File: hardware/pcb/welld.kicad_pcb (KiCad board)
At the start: 2 copper layers, 80 x 55 mm, 126 parts, among them J1 LiPo, J10 PROG, J12 Solar, J2 USB-C, J3 U.FL, J4 4-20mA_1, J5 4-20mA_2, J6 DS18B20, J7 Spare, J8 I2C, J9 GPIO, Q1 BSS123, Q2 BSS123, Q3 BSS84, SW1 RESET, SW2 BOOT, U1 TPS7A0533, U10 MAX17048, U2 TP4056, U3 S-8261A, U4 FS8205A, U5 USBLC6, U6 ESP32-C6, U7 CN3791, U8 TPS61023, U9 ADS1115

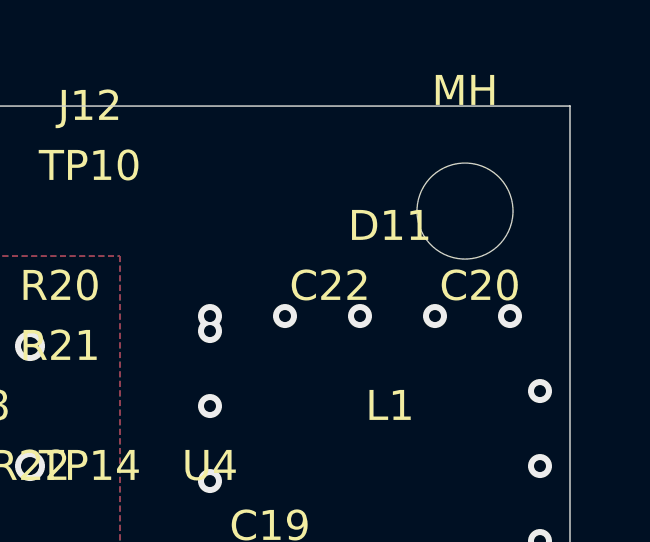
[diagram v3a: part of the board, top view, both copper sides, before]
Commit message: feat(pcb): generate KiCad 10-compatible schematic with working GUI symbol rendering
Rewrote generate_kicad.py to produce lib_symbols entries with the full
"Library:Name" prefix required by KiCad 10's GUI (e.g. "Device:R",
"welld:AP63205WU", "power:VBAT"). kicad-cli tolerates bare names but
the GUI showed "??" for every symbol without the prefix.

Also adds: stdlib symbol embedding (_extract_sym + _STDLIB_NEEDED),
custom VBAT power symbol, welld.kicad_sym library file, project-level
sym-lib-table with absolute paths, and kicad-cli post-upgrade step.

Removes stale jlcpcb_bom.csv / jlcpcb_cpl.csv (superseded by welld_bom.csv).

Co-Authored-By: Claude Sonnet 4.6 <noreply@anthropic.com>
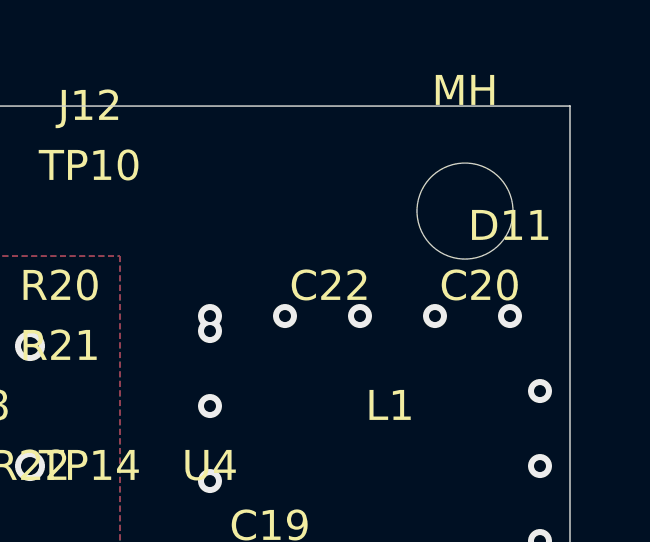
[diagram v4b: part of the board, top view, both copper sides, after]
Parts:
- moved D11 4.00 mm to (78.0, 6.00)
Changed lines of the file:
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@@
-(kicad_pcb (version 20221018) (generator "welld_generate_kicad")
+(kicad_pcb (version 20260206) (generator "pcbnew") (generator_version "10.0")
   (general
     (thickness 1.6)
@@
   (paper "A3")
   (title_block
-    (title "WellD Well-Level Monitor PCB — 2S 18650 LiPo")
+    (title "WellD Well-Level Monitor PCB")
     (date "2026-05-18")
     (company "WellD Project")
@@
   (net 2 "+3V3")
   (net 3 "VBAT")
+  (net 4 "VUSB")
+  (net 5 "VUSB_IN")
   (net 6 "VSOLAR")
   (net 7 "VSOLAR_IN")
@@
   (net 18 "BOOT")
   (net 19 "MPPT_REF")
+  (net 20 "/CHRG_USB")
+  (net 21 "/DONE_USB")
   (net 22 "/CHRG_SOLAR")
+  (net 23 "/DONE_SOLAR")
   (net 24 "VLOOP")
   (net 25 "VBOOST_EN")
+  (net 26 "CHRG_USB_DIS")
   (net 27 "SOLAR_DET")
   (net 28 "BATT_DIV_EN")
   (net 29 "ADS_DRDY")
+  (net 30 "MAX_ALRT")
   (net 31 "LOOP_TERM_CH1")
   (net 32 "LOOP_TERM_CH2")
@@
     )
   )
-  (footprint "Diode_SMD:D_SMA" (layer "F.Cu") (at 74.000 6.000 0.0)
+  (footprint "Diode_SMD:D_SMA" (layer "F.Cu") (at 78.000 6.000 0.0)
     (property "Reference" "D11" (at 0 -2 0) (layer "F.SilkS")
       (effects (font (size 1 1) (thickness 0.15)))
@@
     (connect_pads thru_hole_only (clearance 0.2))
     (min_thickness 0.25)
-    (keepout_settings (no_tracks no) (no_vias no) (no_pads no) (no_copperpour no) (no_footprints no))
     (fill yes (thermal_gap 0.3) (thermal_bridge_width 0.3))
     (polygon
@@
     (connect_pads thru_hole_only (clearance 0.2))
     (min_thickness 0.25)
-    (keepout_settings (no_tracks no) (no_vias no) (no_pads no) (no_copperpour no) (no_footprints no))
     (fill yes (thermal_gap 0.3) (thermal_bridge_width 0.3))
     (polygon

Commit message: hw(pcb): full placement pass, XT30 connector, SMA antenna, BOM cleanup
Component placement:
- All 116 components placed inside 80×55 mm board outline
- pcbway_cpl.csv fully rewritten with correct board-relative coordinates

Battery connector (J1):
- Changed from JST PH 2.0mm to AMASS XT30PW-F right-angle THT (LCSC C601498)
- Pad drill corrected 1.5 mm → 1.8 mm for IPC-2221 wave-solder clearance

Antenna (J3 + W1):
- J3: Amphenol 132289 SMD edge-launch SMA on bottom board edge
- W1: Taoglas CAB.100.07.0050B ~50 mm U.FL-to-SMA pigtail (hand-attached post-reflow)
- RF_ANT net assigned to J3 signal pad

Inductor L2:
- Footprint corrected from L_2512_6332Metric to L_Vishay_IFSC-1515AH_4x4x1.8mm
- Now matches MPN CDRH4D22NP-4R7NC body; shares footprint, reel, and LCSC C376098 with L1

VLOOP output caps (C20, C22):
- Voltage rating upgraded 16 V → 25 V (2.1× margin on 12 V rail; proper DC-bias headroom)
- Footprints unchanged (1206 / 0805)

BOM cleanup:
- J8, J9: marked DNF (expansion headers not populated in production)
- J4–J7, J12, J10: Package updated to THT; PCBWay wave-solders

Case:
- XT30PW-F left-wall cutout added: 14×12 mm slot at Y=17–31 mm, Z=19.3–31.3 mm
- SMA bottom-wall cutout (10.5 mm ⌀ at X=42.5 mm) confirmed present

Co-Authored-By: Claude Sonnet 4.6 <noreply@anthropic.com>
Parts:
- removed C1, C2: 10uF, Capacitor_SMD:C_0805_2012Metric
- removed C16: 4.7uF, Capacitor_SMD:C_0805_2012Metric
- removed C25, C26: 100nF, Capacitor_SMD:C_0402_1005Metric
- removed D2: LED_CHRG, LED_SMD:LED_0603_1608Metric
- removed D3: LED_STBY, LED_SMD:LED_0603_1608Metric
- removed F1: PTC_1A, Fuse:Fuse_1206_3216Metric
- removed J2: USB-C, welld:USB_C_9x3.2mm
- removed the MH at (3.50, 3.50)
- removed the MH at (76.5, 3.50)
- removed the MH at (3.50, 51.5)
- removed the MH at (76.5, 51.5)
- removed Q1: BSS123, Package_TO_SOT_SMD:SOT-23
- removed Q3: BSS84, Package_TO_SOT_SMD:SOT-23
- removed R1: 2k0, Resistor_SMD:R_0402_1005Metric
- removed R15, R16: 5k1, Resistor_SMD:R_0402_1005Metric
- removed R17, R18: 1k_DNF, Resistor_SMD:R_0402_1005Metric
- removed R25, R27, R29: 4k7, Resistor_SMD:R_0402_1005Metric
- removed R30: 10k, Resistor_SMD:R_0402_1005Metric
- removed TP13: MAX_ALRT, TestPoint:TestPoint_Pad_1.0x1.0mm
- removed U10: MAX17048, Package_TO_SOT_SMD:SOT-23-6
- removed U2: TP4056, Package_SO:SOIC-8_3.9x4.9mm_P1.27mm
- removed U3: S-8261A, Package_TO_SOT_SMD:SOT-23-6
- removed U4: FS8205A, Package_TO_SOT_SMD:SOT-23-6
- removed U5: USBLC6, Package_TO_SOT_SMD:SOT-23-6
- added C27: 4.7uF, Capacitor_SMD:C_0805_2012Metric, F.Cu at (90.0, 74.5)
- added C28: 10uF, Capacitor_SMD:C_0805_2012Metric, F.Cu at (93.0, 86.5)
- added C29: 10uF, Capacitor_SMD:C_0805_2012Metric, F.Cu at (93.0, 90.5)
- added C_BST: 100nF, Capacitor_SMD:C_0402_1005Metric, F.Cu at (101.0, 85.5)
- added C_BUCK: 10uF, Capacitor_SMD:C_0805_2012Metric, F.Cu at (90.0, 81.5)
- added D12: PRTR5V, Package_TO_SOT_SMD:SOT-363_SC-70-6, F.Cu at (122.0, 82.5)
- added D13: SMAJ10CA, Diode_SMD:D_SMA, F.Cu at (71.0, 86.5)
- added D14: SMAJ28CA, Diode_SMD:D_SMA, F.Cu at (130.0, 52.5)
- added F2: Polyfuse, Fuse:Fuse_1206_3216Metric, F.Cu at (90.0, 70.5)
- added J13: USB-C, Connector_USB:USB_C_Receptacle_GCT_USB4135-GF-A_6P_TopMnt_Horizontal, F.Cu at (70.0, 71.5)
- added L2: 4.7uH, Inductor_SMD:L_Vishay_IFSC-1515AH_4x4x1.8mm, F.Cu at (82.0, 80.5)
- added MH: MountingHole_3.2mm_M3, MountingHole:MountingHole_3.2mm_M3, F.Cu at (68.5, 50.0)
- added MH: MountingHole_3.2mm_M3, MountingHole:MountingHole_3.2mm_M3, F.Cu at (141.5, 50.0)
- added MH: MountingHole_3.2mm_M3, MountingHole:MountingHole_3.2mm_M3, F.Cu at (68.5, 98.0)
- added MH: MountingHole_3.2mm_M3, MountingHole:MountingHole_3.2mm_M3, F.Cu at (141.5, 98.0)
- added R33: 604k, Resistor_SMD:R_0402_1005Metric, F.Cu at (92.0, 60.5)
- added R34: 100k, Resistor_SMD:R_0402_1005Metric, F.Cu at (92.0, 64.5)
- added R35: 1k2, Resistor_SMD:R_0402_1005Metric, F.Cu at (81.0, 86.5)
- added R36: 100k, Resistor_SMD:R_0402_1005Metric, F.Cu at (81.0, 90.5)
- added R37: 4k7, Resistor_SMD:R_0402_1005Metric, F.Cu at (81.0, 94.5)
- added R38: 4k7, Resistor_SMD:R_0402_1005Metric, F.Cu at (86.0, 94.5)
- added R_CC1: 5k1, Resistor_SMD:R_0402_1005Metric, F.Cu at (78.0, 69.5)
- added R_CC2: 5k1, Resistor_SMD:R_0402_1005Metric, F.Cu at (78.0, 72.5)
- added TP15: CHRG_USB, TestPoint:TestPoint_Pad_1.0x1.0mm, F.Cu at (132.0, 98.5)
- added U11: USBLC6, Package_TO_SOT_SMD:SOT-23-6, F.Cu at (84.0, 70.5)
- added U12: TP5100, Package_SO:SOIC-8_3.9x4.9mm_P1.27mm, F.Cu at (86.0, 89.5)
- C20: value 22uF -> 22uF 25V
- C22: value 10uF -> 10uF 25V
- D1: value PRTR5V0U2X -> PRTR5V
- D10, D9: value SMAJ3.3CA -> SMAJ3.3
- D11: value SMAJ13A -> SMAJ13
- D4: value LED_STATUS -> Status
- D7: value LED_SOLAR -> LED
- D8: value SMAJ7.0A -> SMAJ28CA
- FB1: value 600R@100MHz -> Ferrite; footprint Ferrite_Bead_SMD:L_0402_1005Metric -> Inductor_SMD:L_0402_1005Metric
- J1: value LiPo -> XT30PW-F; footprint Connector_JST:JST_XH_B2B-XH-AM_1x02_P2.50mm_Horizontal -> WellD:XT30PW-F_RightAngle
- J12: footprint Connector_Phoenix_MC:PhoenixContact_MC_1,5_2-G-3,5_1x02_P3.50mm_Horizontal -> TerminalBlock_Phoenix:TerminalBlock_Phoenix_PT-1,5-2-3.5-H_1x02_P3.50mm_Horizontal
- J3: value U.FL -> 132289; footprint Connector_Coaxial:U.FL_Hirose_U.FL-R-SMT-1_Vertical -> Connector_Coaxial:SMA_Amphenol_132289_EdgeMount
- J4, J5, J6, J7: footprint Connector_Phoenix_MC:PhoenixContact_MC_1,5_3-G-3,5_1x03_P3.50mm_Horizontal -> TerminalBlock_Phoenix:TerminalBlock_Phoenix_PT-1,5-3-3.5-H_1x03_P3.50mm_Horizontal
- L1: footprint Inductor_SMD:L_1812_4532Metric -> Inductor_SMD:L_Vishay_IFSC-1515AH_4x4x1.8mm
- R2, R4: value 100R_0.1% -> 100R
- R22: value 1k_DNF -> 1k DNF
- R23: value 1.1M -> 1.91M
- R24: value 47k -> 100k
- R32: value 33R_DNF -> 33R
- R7: value 100k -> 330k
- SJ1: value VBOOST_EN -> VBOOST; footprint Jumper:SolderJumper-2_P1.3mm_Open_RoundedPad1.0x1.5mm -> Jumper:SolderJumper-2_P1.3mm_Open_Pad1.0x1.5mm
- SJ2: value VLOOP_BUS -> VLOOP; footprint Jumper:SolderJumper-2_P1.3mm_Open_RoundedPad1.0x1.5mm -> Jumper:SolderJumper-2_P1.3mm_Open_Pad1.0x1.5mm
- SJ3, SJ4, SJ5: footprint Jumper:SolderJumper-2_P1.3mm_Open_RoundedPad1.0x1.5mm -> Jumper:SolderJumper-2_P1.3mm_Open_Pad1.0x1.5mm
- SW1, SW2: footprint Button_Switch_SMD:SW_SPST_TL3305AF160QG -> Button_Switch_SMD:SW_Push_1P1T_NO_CK_KSC6xxG
- TP10: value VSOLAR_IN -> VSOLAR
- TP14: value /CHRG_SOLAR -> CHRG_SOL
- TP5: value LOOP_TERM_CH1 -> LOOP1
- TP6: value LOOP_TERM_CH2 -> LOOP2
- TP8: value I2C_SDA -> SDA
- TP9: value I2C_SCL -> SCL
- U1: value TPS7A0533 -> AP63205; footprint Package_TO_SOT_SMD:SC-70-5 -> Package_TO_SOT_SMD:SOT-23-6
- U6: footprint welld:ESP32_C6_MINI_1U -> PCM_Espressif:ESP32-C6-MINI-1U
- U7: value CN3791 -> CN3722
- U8: value TPS61023 -> MT3608; footprint Package_TO_SOT_SMD:SOT-23-5 -> Package_TO_SOT_SMD:SOT-23-6
- moved J9 297.4 mm to (265.0, 256.5)
- moved J8 279.7 mm to (265.0, 246.5)
- moved J4 140.6 mm to (138.0, 64.5), turned to 180 degrees
- moved J5 137.0 mm to (138.0, 76.5), turned to 180 degrees
- moved J6 135.3 mm to (138.0, 88.5), turned to 180 degrees
- moved SJ4 132.9 mm to (118.0, 90.5)
- moved J7 132.6 mm to (138.0, 96.5), turned to 180 degrees
- moved R2 131.8 mm to (129.0, 79.5)
- moved D9 131.5 mm to (123.0, 76.5)
- moved SJ5 130.7 mm to (118.0, 94.5)
- moved SJ2 129.8 mm to (113.0, 94.5)
- moved C_SH1 129.2 mm to (129.0, 76.5)
- moved R4 128.9 mm to (129.0, 87.5)
- moved D10 127.1 mm to (123.0, 84.5)
- moved C4 127.0 mm to (129.0, 82.5)
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
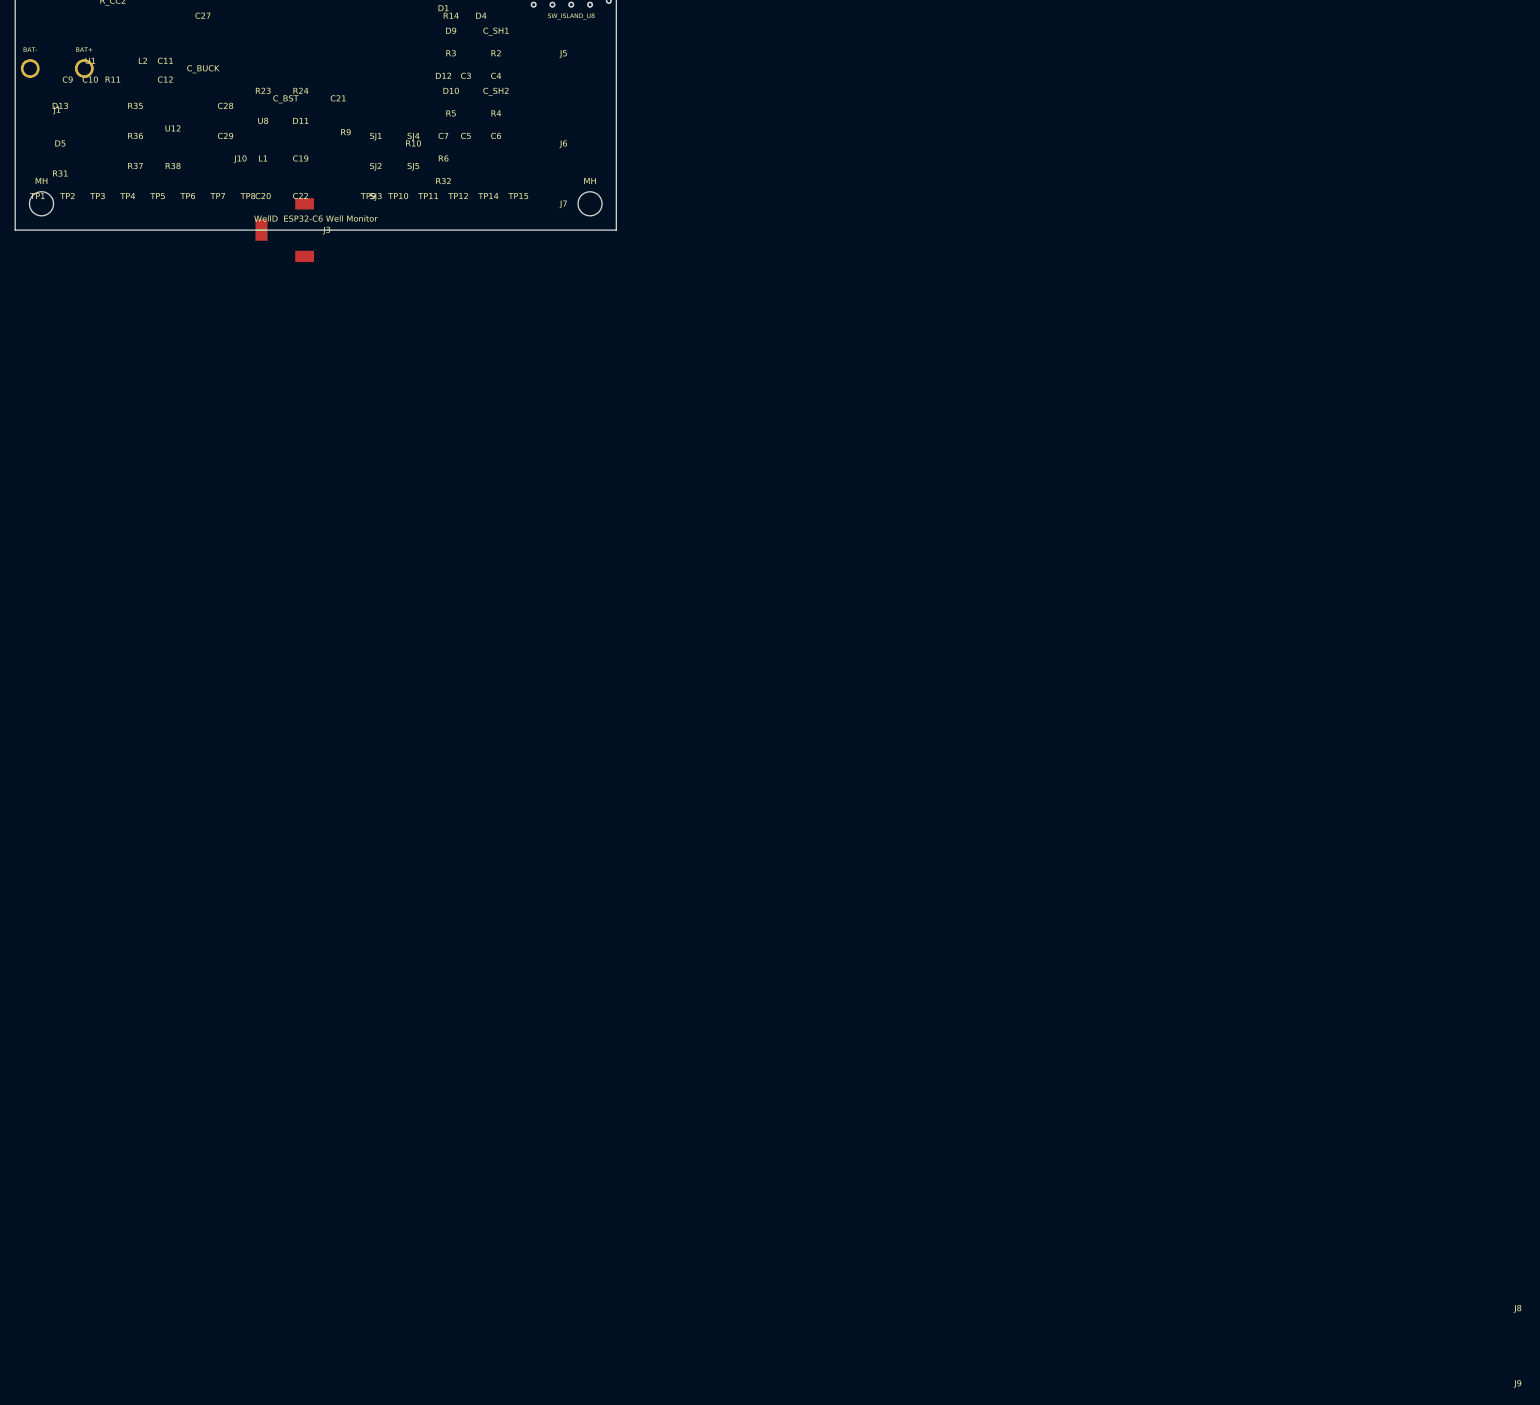
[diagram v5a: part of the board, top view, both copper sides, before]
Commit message: hw(pcb): fix J1 XT30 placement — rotation 270°, correct pad names/drill
The community AMASS_XT30PW-M footprint has pads at y=10mm (10mm from
the connector face) and 5mm pin pitch. To mount at the left wall with
the mating face pointing outward, J1 needs rotation 270°, not 180°.

- Footprint: rename pads P→1, N→2 to match schematic pin numbers;
  drill 1.7→1.8mm (our IPC-2221 spec)
- generate_kicad.py: J1 board pos (5.6,33.5)→(2.0,33.5), rot 180→270;
  update courtyard keepout comment
- Regenerate welld.kicad_pcb: J1 now at PCB (67,80) @270°

At 270° from board (2,33.5): mating face at board x≈-1mm (accessible
through left-wall case cutout), power pins at board (12,31)+(12,36),
courtyard X -1.2..13.5, Y 26.6..40.4. Case cutout Y unchanged.

Co-Authored-By: Claude Sonnet 4.6 <noreply@anthropic.com>
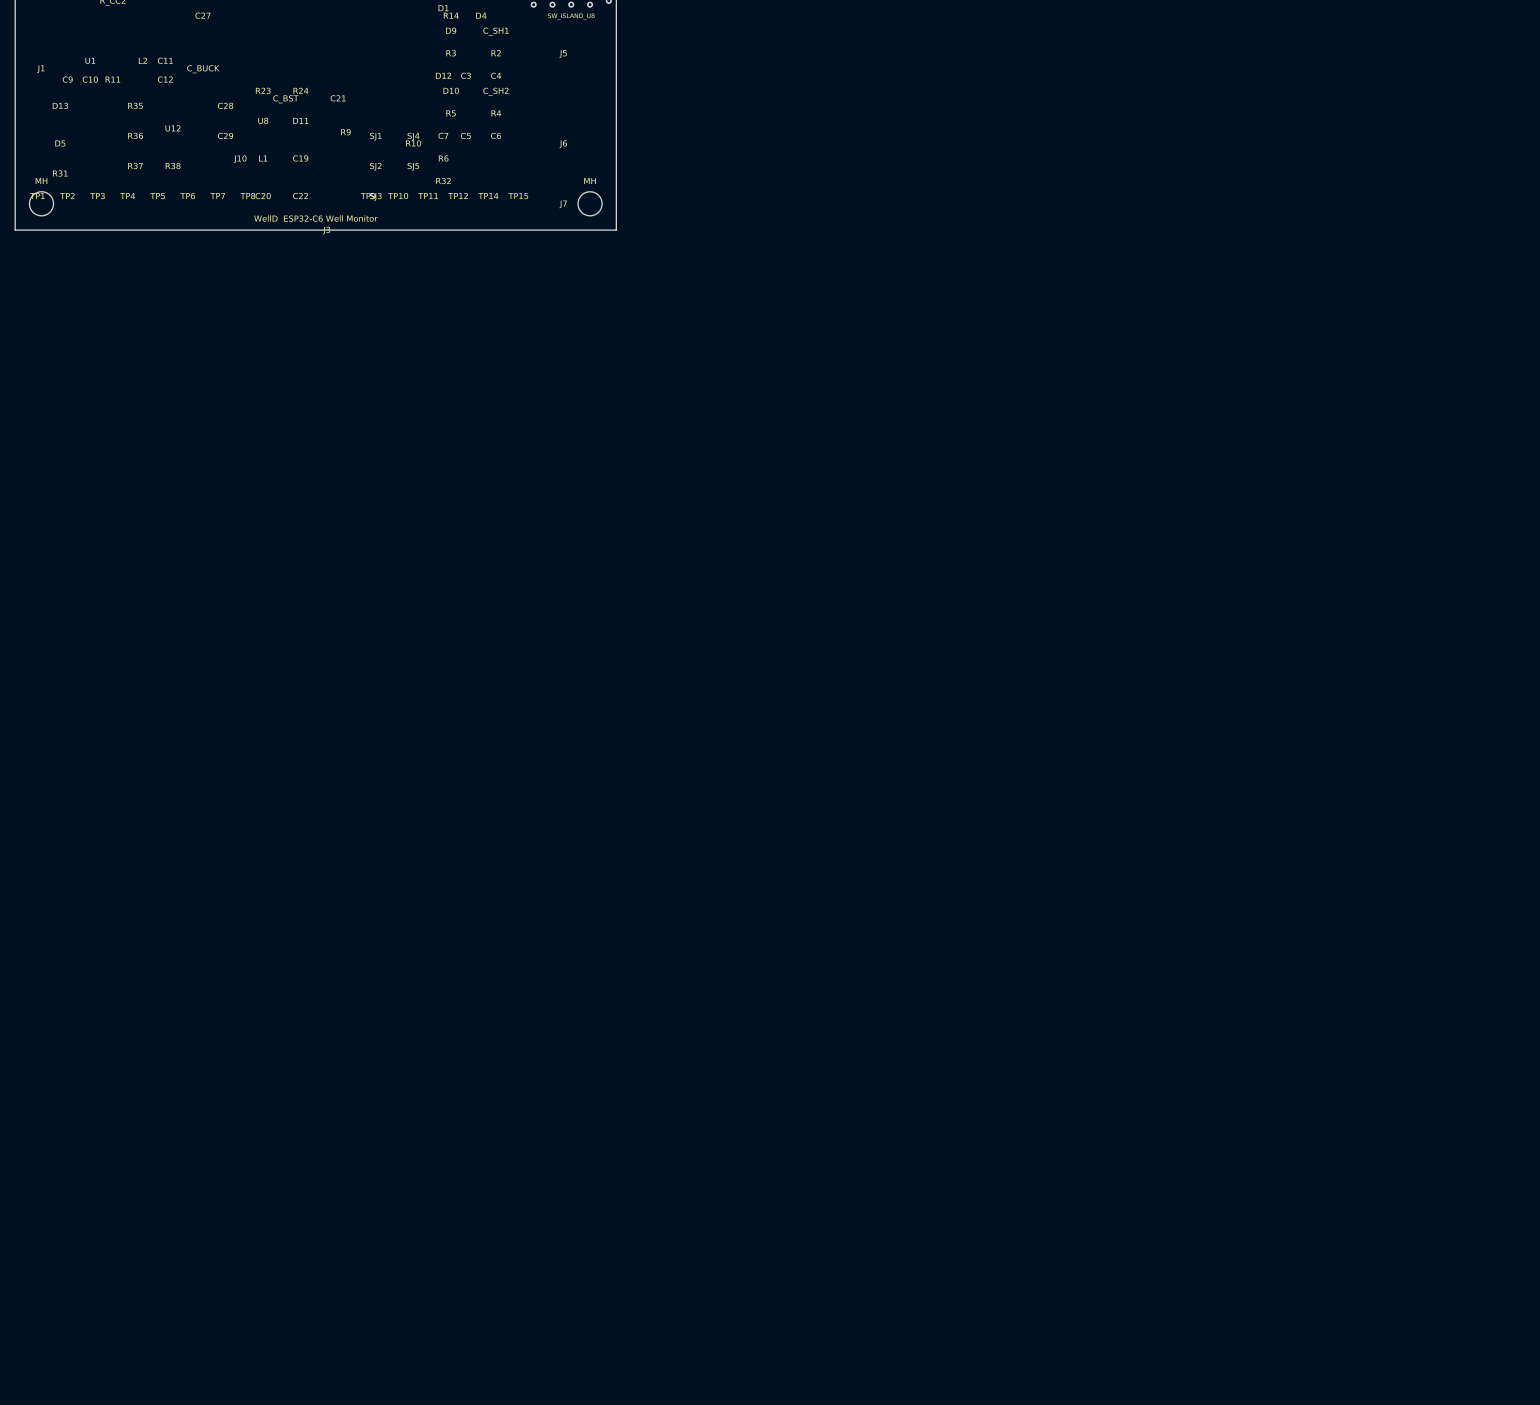
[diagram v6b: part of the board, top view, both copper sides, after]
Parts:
- removed J8: I2C, Connector_PinHeader_2.54mm:PinHeader_1x04_P2.54mm_Vertical
- removed J9: GPIO, Connector_PinHeader_2.54mm:PinHeader_1x08_P2.54mm_Vertical
- C10: value 1uF -> 100nF
- U8: value MT3608 -> MT3608B
- moved J1 3.60 mm to (67.0, 80.0), turned to 270 degrees
